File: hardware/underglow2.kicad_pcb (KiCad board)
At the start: 4 copper layers, 78.5 x 95 mm, 96 parts, among them J101 J_Delphi_Sicma_24, J501 Conn_ARM_SWD_TagConnect_TC203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, J502 Conn_ARM_SWD_TagConnect_TC2030, J601 Conn_ARM_SWD_TagConnect_TC203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, Q301 AO4803A, Q302 8205A, Q303 8205A, Q304 8205A, Q305 BCX56, Q306 BCX56, U201 TPS62172DSGR, U301 MCP1416, U302 MCP1416, U303 MCP1416, U304 MCP1416, U305 MCP1416, U306 MCP1416, U307 MCP1416, U308 MCP1416, U401 TLE9251VSJXUMA1, U501 STM32G431CBU6, U601 DA14531-00000FX2, U801 RF69, Y501 32_Mhz, Y601 32_Mhz, Y801 32_Mhz

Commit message: Update layout
Signed-off-by: Connor Rigby <connorr@hey.com>
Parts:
- moved C801 4.50 mm to (31.5, 95.5)
- moved C813 4.50 mm to (27.0, 95.5)
- moved C815 4.50 mm to (39.7, 94.0)
- moved U801 4.50 mm to (35.8, 92.3)
- moved C810 4.50 mm to (29.3, 88.7)
- moved C811 4.50 mm to (29.3, 89.9)
- moved C812 4.50 mm to (29.3, 91.1)
- moved Y801 4.50 mm to (29.3, 94.0)
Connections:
- U501 pad 9: unconnected-(U501-PA1-Pad9) -> /Application/PIXEL_2_PWM
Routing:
- net /Application/PIXEL_2_PWM: track 88.3 -> 130.2 mm, vias 1 -> 4
- net unconnected-(U501-PA1-Pad9): track 22.5 -> 0.00 mm, vias 2 -> 0
- net unconnected-(U501-PA0-Pad8): track 20.4 -> 0.00 mm, vias 2 -> 0
- net unconnected-(U501-PB6-Pad44): track 16.2 -> 0.00 mm, vias 2 -> 0
- net unconnected-(U501-PB7-Pad45): track 15.0 -> 0.00 mm, vias 2 -> 0
- net unconnected-(U501-PC13-Pad2): track 7.10 -> 0.00 mm, vias 1 -> 0
- net /Application/SPI1_SCK: track 24.8 -> 29.6 mm
- net /Application/SPI1_MOSI: track 43.0 -> 47.8 mm
- net /Application/SPI1_RESET: track 39.6 -> 44.1 mm
- net /Application/SPI1_IRQ: track 36.1 -> 40.6 mm
- net /Application/SPI1_MISO: track 25.2 -> 29.7 mm
- net /Application/SPI1_NSS: track 23.2 -> 27.4 mm
- net +3.3V: track 220.8 -> 224.4 mm
- net /Application/RGB1_B_PWM: track 69.4 -> 72.5 mm
- net GND: track 140.1 -> 142.3 mm, vias 56 -> 57
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- removed copper zone on B.Cu, net GND

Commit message: layout updates
Signed-off-by: Connor Rigby <connorr@hey.com>
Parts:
- added ANT601: BWIPX-1-001E, LCSC_Antenna:IPEX-SMD_BWIPX-1-001E, F.Cu at (71.8, 97.0)
- added ANT801: BWSMA-KE-P001, LCSC_Antenna:SMA-SMD_BWSMA-KE-P001, F.Cu at (33.8, 21.6)
- added C605: C_0402_DNP, Capacitor_SMD:C_0402_1005Metric, F.Cu at (77.8, 97.5)
- added C606: C_0402_DNP, Capacitor_SMD:C_0402_1005Metric, F.Cu at (74.6, 97.5)
- added C801: C_0805_10u_X5R, Capacitor_SMD:C_0805_2012Metric, F.Cu at (27.1, 88.7)
- added C802: C_0402_DNP, Capacitor_SMD:C_0402_1005Metric, F.Cu at (35.7, 80.0)
- added C803: C_0402_DNP, Capacitor_SMD:C_0402_1005Metric, F.Cu at (34.7, 80.0)
- added C804: C_0402_DNP, Capacitor_SMD:C_0402_1005Metric, F.Cu at (35.1, 81.5)
- added C805: C_0402_DNP, Capacitor_SMD:C_0402_1005Metric, F.Cu at (33.7, 83.0)
- added C806: C_0402_DNP, Capacitor_SMD:C_0402_1005Metric, F.Cu at (34.7, 85.0)
- added C807: C_0402_DNP, Capacitor_SMD:C_0402_1005Metric, F.Cu at (35.1, 86.5)
- added C808: C_0402_DNP, Capacitor_SMD:C_0402_1005Metric, F.Cu at (33.6, 88.1)
- added C809: C_0402_DNP, Capacitor_SMD:C_0402_1005Metric, F.Cu at (32.5, 88.1)
- added C816: C_0402_DNP, Capacitor_SMD:C_0402_1005Metric, F.Cu at (39.0, 88.1)
- added C817: C_0402_DNP, Capacitor_SMD:C_0402_1005Metric, F.Cu at (37.4, 86.5)
- added C818: C_0402_DNP, Capacitor_SMD:C_0402_1005Metric, F.Cu at (37.9, 85.0)
- added C819: C_0402_DNP, Capacitor_SMD:C_0402_1005Metric, F.Cu at (39.0, 83.0)
- added C820: C_0402_DNP, Capacitor_SMD:C_0402_1005Metric, F.Cu at (37.4, 81.5)
- added C821: C_0402_DNP, Capacitor_SMD:C_0402_1005Metric, F.Cu at (38.9, 80.0)
- added C822: C_0402_DNP, Capacitor_SMD:C_0402_1005Metric, F.Cu at (36.8, 80.0)
- added C823: C_0402_DNP, Capacitor_SMD:C_0402_1005Metric, F.Cu at (36.8, 78.1)
- added C824: C_0402_DNP, Capacitor_SMD:C_0402_1005Metric, F.Cu at (35.7, 78.1)
- added C825: C_0402_DNP, Capacitor_SMD:C_0402_1005Metric, F.Cu at (38.3, 74.3)
- added C826: C_0402_DNP, Capacitor_SMD:C_0402_1005Metric, F.Cu at (34.3, 34.0)
- added C827: C_0402_DNP, Capacitor_SMD:C_0402_1005Metric, F.Cu at (34.3, 31.0)
- added G***: LOGO, LOGO, F.Cu at (56.2, 108.5)
- added L801: L_0402_DNP, Inductor_SMD:L_0402_1005Metric, F.Cu at (33.7, 80.0)
- added L802: L_0402_DNP, Inductor_SMD:L_0402_1005Metric, F.Cu at (34.7, 83.0)
- added L803: L_0402_DNP, Inductor_SMD:L_0402_1005Metric, F.Cu at (34.7, 88.1)
- added L804: L_0402_DNP, Inductor_SMD:L_0402_1005Metric, F.Cu at (35.8, 88.1)
- added L805: L_0402_DNP, Inductor_SMD:L_0402_1005Metric, F.Cu at (36.8, 88.1)
- added L806: L_0402_DNP, Inductor_SMD:L_0402_1005Metric, F.Cu at (37.9, 88.1)
- added L807: L_0402_DNP, Inductor_SMD:L_0402_1005Metric, F.Cu at (37.9, 83.0)
- added L808: L_0402_DNP, Inductor_SMD:L_0402_1005Metric, F.Cu at (37.9, 80.0)
- added Q801: BCX56, Package_TO_SOT_SMD:SOT-89-3, F.Cu at (29.3, 81.8)
- added R601: R_0402_DNP, Resistor_SMD:R_0402_1005Metric, F.Cu at (76.2, 97.0)
- added R801: R_0402_DNP, Resistor_SMD:R_0402_1005Metric, F.Cu at (40.3, 97.2)
- added R802: R_0402_10k, Resistor_SMD:R_0402_1005Metric, F.Cu at (29.9, 85.9)
- added R803: R_0402_DNP, Resistor_SMD:R_0402_1005Metric, F.Cu at (28.8, 85.9)
- added R804: R_0402_DNP, Resistor_SMD:R_0402_1005Metric, F.Cu at (33.8, 32.5)
- added U802: AS193-73LF, Package_TO_SOT_SMD:SOT-363_SC-70-6, F.Cu at (38.8, 76.6)
- renumbered C801 to C814
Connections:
- U801 pad 22: unconnected-(U801-RXTX-Pad22) -> /Radio/RXTX
- U801 pad 24: unconnected-(U801-RFIO-Pad24) -> /Radio/RF_IO
- U801 pad 26: unconnected-(U801-PA_BOOST-Pad26) -> /Radio/PA_BOOST
- U801 pad 27: unconnected-(U801-VR_PA-Pad27) -> /Radio/VR_PA
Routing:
- net /Radio/RXTX: track 0.00 -> 52.1 mm, vias 0 -> 2
- net /Radio/RF69_ANT_MATCH: track 0.00 -> 42.3 mm
- net /Radio/VR_PA: track 0.00 -> 21.6 mm, vias 0 -> 2
- net /Radio/~{RXTX}: track 0.00 -> 17.5 mm
- net GND: track 142.3 -> 156.3 mm, vias 57 -> 129
- net +3.3V: track 224.4 -> 234.3 mm, vias 17 -> 18
- net /Radio/J3: track 0.00 -> 4.98 mm
- net /Radio/RF69_ANTENNA: track 0.00 -> 4.50 mm
- net /BLE/BT_ANT: track 1.21 -> 5.32 mm
- net /Radio/RX_ANT_MATCH: track 0.00 -> 4.06 mm
- net /Radio/TX_ANT_MATCH: track 0.00 -> 3.97 mm
- net /Application/SPI1_RESET: track 44.1 -> 47.9 mm
- net /Radio/RF_IO_MATCH: track 0.00 -> 3.19 mm
- net /Radio/PA_BOOST_MATCH: track 0.00 -> 3.19 mm
- net /Radio/RX_ANT: track 0.00 -> 3.11 mm
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
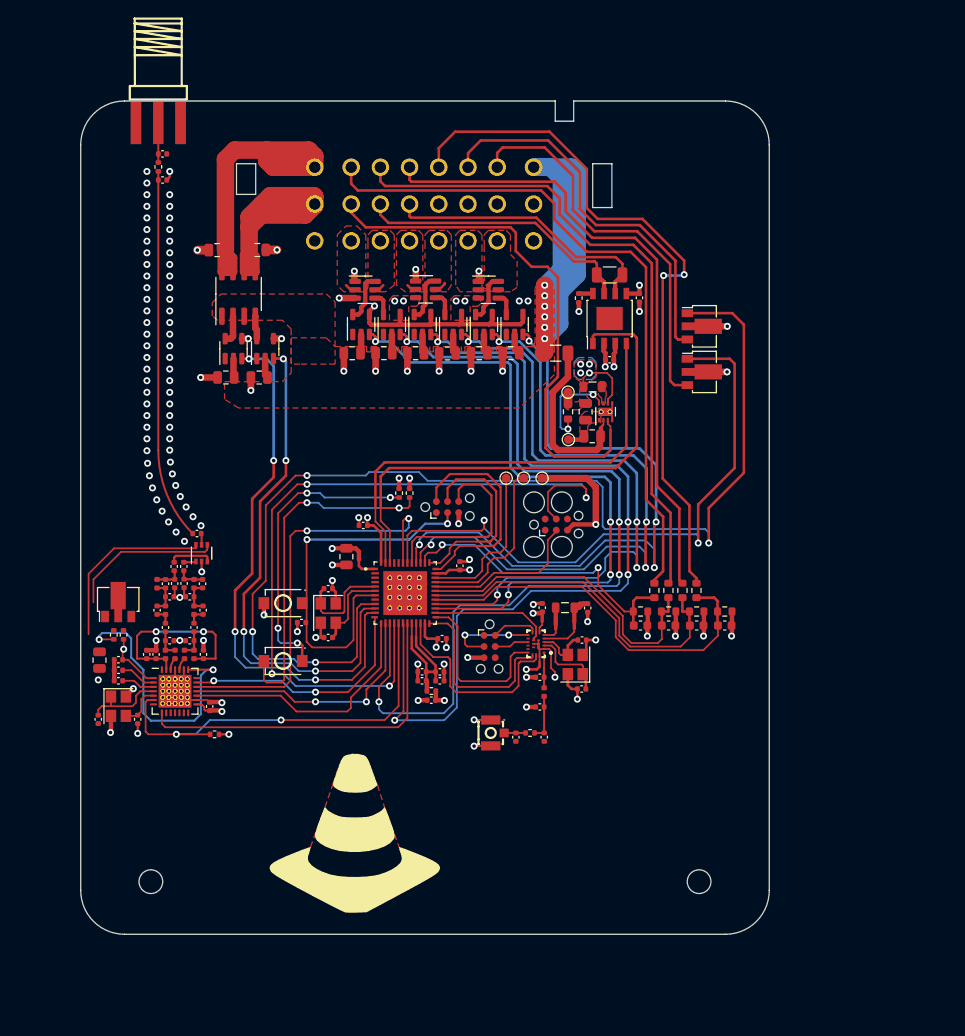
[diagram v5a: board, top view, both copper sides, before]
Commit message: RF layout updates
Signed-off-by: Connor Rigby <connorr@hey.com>
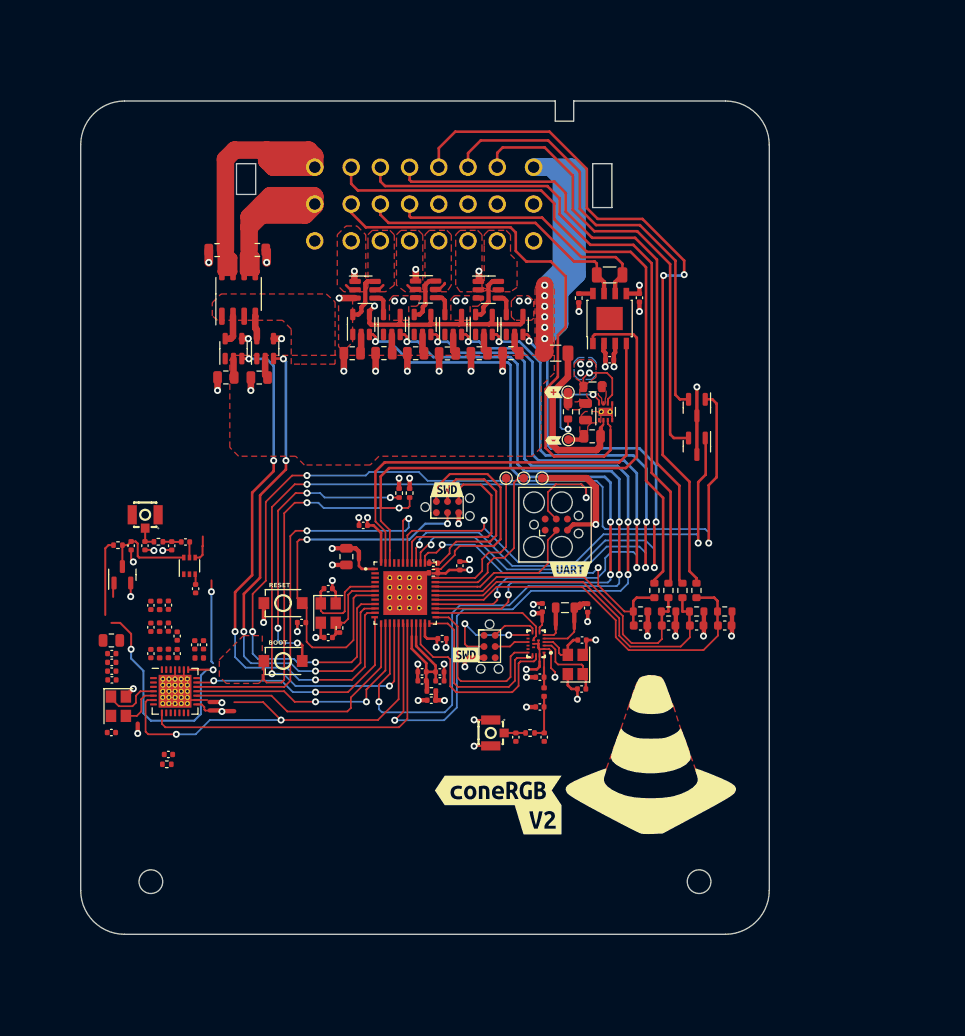
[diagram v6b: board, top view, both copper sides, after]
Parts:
- removed C817, C818, C819, C820, C821, C822, C824: C_0402_DNP, Capacitor_SMD:C_0402_1005Metric
- removed L806, L807, L808: L_0402_DNP, Inductor_SMD:L_0402_1005Metric
- added C828: C_0402_DNP, Capacitor_SMD:C_0402_1005Metric, F.Cu at (30.8, 75.7)
- added C829: C_0402_DNP, Capacitor_SMD:C_0402_1005Metric, F.Cu at (65.2, 77.7)
- added R805: R_0402_10k, Resistor_SMD:R_0402_1005Metric, F.Cu at (65.2, 78.8)
- added kibuzzard-64154474: G***, kibuzzard-64154474, F.Cu at (72.6, 103.6)
- added kibuzzard-6415457F: G***, kibuzzard-6415457F, F.Cu at (77.2, 107.0)
- added kibuzzard-641546EE: G***, kibuzzard-641546EE, F.Cu at (68.9, 88.2)
- added kibuzzard-64154737: G***, kibuzzard-64154737, F.Cu at (80.8, 78.4)
- added kibuzzard-641547A6: G***, kibuzzard-641547A6, F.Cu at (66.8, 69.3)
- added kibuzzard-64155347: G***, kibuzzard-64155347, F.Cu at (78.9, 58.2)
- added kibuzzard-641553AB: G***, kibuzzard-641553AB, F.Cu at (78.9, 63.7)
- ANT801: value BWSMA-KE-P001 -> BWIPX-1-001E; footprint LCSC_Antenna:SMA-SMD_BWSMA-KE-P001 -> LCSC_Antenna:IPEX-SMD_BWIPX-1-001E
- C801: value C_0805_10u_X5R -> C_0402_DNP; footprint Capacitor_SMD:C_0805_2012Metric -> Capacitor_SMD:C_0402_1005Metric
- C808, C809, C813: value C_0402_DNP -> C_0402_100nf_X7R
- C811, C812, C815: value C_0402_100nf_X7R -> C_0402_DNP
- C816: value C_0402_DNP -> C_0805_10u_X5R; footprint Capacitor_SMD:C_0402_1005Metric -> Capacitor_SMD:C_0805_2012Metric
- L801: value L_0402_DNP -> 2.7nh
- L802: value L_0402_DNP -> 22nh
- L803, L804, L805: value L_0402_DNP -> 5.6nh
- Q305, Q306, Q801: value BCX56 -> BC817; footprint Package_TO_SOT_SMD:SOT-89-3 -> Package_TO_SOT_SMD:SOT-23
- moved ANT801 50.7 mm to (32.4, 72.2)
- moved C827 44.7 mm to (32.3, 75.7), turned to 90 degrees
- moved R804 42.7 mm to (33.9, 75.2), turned to 180 degrees
- moved C826 41.7 mm to (35.4, 75.7), turned to 90 degrees
- moved G*** 34.9 mm to (90.0, 99.5)
- moved R803 25.7 mm to (54.5, 85.1)
- moved C814 11.3 mm to (39.0, 87.0)
- moved C816 10.6 mm to (28.5, 86.5), turned to 180 degrees
- moved R802 10.2 mm to (29.2, 75.6), turned to 0 degrees
- moved Q306 9.28 mm to (95.2, 60.0), turned to -90 degrees
- moved C813 8.94 mm to (35.0, 99.5), turned to 0 degrees
- moved Q305 8.49 mm to (95.2, 64.4), turned to -90 degrees
- moved L801 8.05 mm to (35.0, 88.0), turned to 90 degrees
- moved C802 7.99 mm to (36.0, 88.0)
- moved C815 7.22 mm to (38.0, 87.0), turned to -90 degrees
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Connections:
- ANT801 pad 1: GND -> /Radio/RF69_ANTENNA
- C801 pad 1: +3.3V -> /Radio/VR_PA
- C802 pad 1: /Radio/TX_ANT -> Net-(C802-Pad1)
- C803 pad 1: /Radio/TX_ANT -> Net-(C802-Pad1)
- C803 pad 2: /Radio/TX_ANT_MATCH -> Net-(C803-Pad2)
- C804 pad 1: /Radio/TX_ANT_MATCH -> Net-(C803-Pad2)
- C804 pad 2: GND -> Net-(C804-Pad2)
- C805 pad 1: /Radio/TX_ANT_MATCH -> GND
- C805 pad 2: /Radio/PA_BOOST_RF -> Net-(C804-Pad2)
- C806 pad 1: /Radio/PA_BOOST_RF -> Net-(C804-Pad2)
- C806 pad 2: /Radio/PA_BOOST_MATCH -> /Radio/J2
- C807 pad 1: /Radio/PA_BOOST_MATCH -> GND
- C807 pad 2: GND -> /Radio/J2
- C808 pad 1: /Radio/VR_PA -> +3.3V
- C809 pad 1: /Radio/VR_PA -> /Radio/VR_ANA
- C810 pad 1: +3.3V -> /Radio/VR_DIG
- C811 pad 1: /Radio/VR_ANA -> /Radio/XTA
- C812 pad 1: /Radio/VR_DIG -> /Radio/XTB
- C813 pad 1: /Radio/XTA -> +3.3V
- C814 pad 1: /Radio/XTB -> Net-(C814-Pad1)
- C815 pad 1: +3.3V -> Net-(C814-Pad1)
- C815 pad 2: GND -> /Radio/RF_IO
- C816 pad 1: /Radio/VR_PA -> +3.3V
- C823 pad 1: /Radio/RX_ANT -> Net-(C814-Pad1)
- C823 pad 2: /Radio/J2 -> /Radio/J3
- C825 pad 1: /Radio/J1 -> unconnected-(C825-Pad1)
- L801 pad 1: /Radio/TX_ANT -> /Radio/PA_BOOST
- L801 pad 2: /Radio/TX_ANT_MATCH -> Net-(C802-Pad1)
- L802 pad 1: /Radio/TX_ANT_MATCH -> /Radio/VR_PA
- L802 pad 2: /Radio/PA_BOOST_RF -> Net-(C802-Pad1)
- L803 pad 1: /Radio/PA_BOOST_MATCH -> Net-(C803-Pad2)
- L803 pad 2: /Radio/VR_PA -> Net-(C804-Pad2)
- L804 pad 1: /Radio/PA_BOOST_MATCH -> Net-(C804-Pad2)
- L804 pad 2: /Radio/PA_BOOST -> /Radio/J2
- L805 pad 1: /Radio/RF_IO -> GND
- L805 pad 2: /Radio/RF_IO_MATCH -> /Radio/RF_IO
- Q305 pad 2: +3.3V -> /RGB/PIXEL_1
- Q305 pad 3: /RGB/PIXEL_1 -> +3.3V
- Q306 pad 2: +3.3V -> /RGB/PIXEL_2
- Q306 pad 3: /RGB/PIXEL_2 -> +3.3V
- Q801 pad 1: /Radio/RXTX_INV -> unconnected-(Q801-B-Pad1)
- Q801 pad 2: /Radio/~{RXTX} -> GND
- Q801 pad 3: GND -> Net-(Q801-C)
- R802 pad 2: /Radio/~{RXTX} -> Net-(Q801-C)
- U802 pad 4: /Radio/~{RXTX} -> unconnected-(U802-V2-Pad4)
- U802 pad 5: /Radio/J1 -> unconnected-(U802-J1-Pad5)
- U802 pad 6: /Radio/RXTX -> Net-(Q801-C)
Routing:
- net /Radio/RF69_ANT_MATCH: track 42.3 -> 2.12 mm
- net /Radio/RXTX: track 52.1 -> 28.5 mm
- net /Radio/VR_PA: track 21.6 -> 0.00 mm, vias 2 -> 0
- net /Radio/~{RXTX}: track 17.5 -> 0.00 mm
- net /Application/PIXEL_2_PWM: track 130.2 -> 114.6 mm
- net /Application/PIXEL_1_PWM: track 70.1 -> 54.6 mm
- net Net-(Q801-C): track 0.00 -> 11.2 mm
- net unconnected-(R805-Pad1): track 0.00 -> 9.54 mm, vias 0 -> 1
- net GND: track 156.3 -> 148.4 mm, vias 129 -> 62
- net /RGB/PIXEL_2: track 44.2 -> 51.0 mm
- net /RGB/PIXEL_1: track 44.9 -> 51.1 mm
- net /Radio/VR_ANA: track 4.09 -> 0.00 mm
- net /Radio/RX_ANT_MATCH: track 4.06 -> 0.00 mm
- net /Radio/TX_ANT_MATCH: track 3.97 -> 0.00 mm
- net /Radio/VR_DIG: track 3.80 -> 0.00 mm
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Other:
- board text added: "BOOT"
- board text added: "RESET"

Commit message: Almost ready for fab
Signed-off-by: Connor Rigby <connorr@hey.com>
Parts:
- added D201: LED_0603_RED, LED_SMD:LED_0603_1608Metric, F.Cu at (78.9, 62.4)
- added D501: LED_0603_GREEN, LED_SMD:LED_0603_1608Metric, F.Cu at (50.7, 78.6)
- added D502: LED_0603_YELLOW, LED_SMD:LED_0603_1608Metric, F.Cu at (52.3, 78.6)
- added R201: R_0603_330, Resistor_SMD:R_0603_1608Metric, F.Cu at (78.9, 59.3)
- added R503: R_0603_330, Resistor_SMD:R_0603_1608Metric, F.Cu at (50.7, 75.5)
- added R504: R_0603_330, Resistor_SMD:R_0603_1608Metric, F.Cu at (52.3, 75.5)
- added kibuzzard-6418DACD: G***, kibuzzard-6418DACD, F.Cu at (48.6, 74.8)
- added kibuzzard-6418DAF6: G***, kibuzzard-6418DAF6, F.Cu at (54.5, 74.8)
- added kibuzzard-6418DF1A: G***, kibuzzard-6418DF1A, F.Cu at (76.5, 63.0)
- C503, C504, C603, C604, C811, C812: value C_0402_DNP -> C_0402_33p_C0G
- C801: value C_0402_DNP -> C_0402_10n_C0G
- C802: value C_0402_DNP -> C_0402_8p2_C0G
- C803: value C_0402_DNP -> C_0402_22p_C0G
- C805: value C_0402_DNP -> C_0402_6p8_C0G
- C807: value C_0402_DNP -> C_0402_3p3_C0G
- C814: value C_0402_DNP -> C_0402_5p6_C0G
- C815: value C_0402_DNP -> L_0402_5n6; footprint Capacitor_SMD:C_0402_1005Metric -> Inductor_SMD:L_0402_1005Metric
- C823, C825: value C_0402_DNP -> C_0402_100p_C0G
- C828, C829: value C_0402_DNP -> C_0402_1nf_X7R
- L501, R601, R804: value R_0402_DNP -> R_0402_0
- L801: value 2.7nh -> L_0402_2n7
- L802: value 22nh -> L_0402_22n
- L803, L804: value 5.6nh -> L_0402_5n6
- L805: value 5.6nh -> L_0402_120n
- R701, R703, R705, R707: value DNP -> R_0603_100k
- R702, R704, R706, R708: value DNP -> R_0603_20k
- R801, R803: value R_0402_DNP -> R_0402_100k
- R802: value R_0402_10k -> R_0402_100k
- moved R805 35.0 mm to (31.0, 86.0), turned to 90 degrees
- moved C829 26.5 mm to (38.7, 78.8)
- moved R803 16.7 mm to (38.7, 79.8), turned to 180 degrees
- moved R801 10.0 mm to (42.2, 93.8), turned to 90 degrees
- moved C813 7.48 mm to (39.9, 93.8), turned to 90 degrees
- moved C828 5.03 mm to (29.2, 80.5), turned to 0 degrees
- moved C823 4.00 mm to (38.1, 84.6)
- moved Q801 4.00 mm to (29.8, 83.0)
- moved U802 4.00 mm to (37.4, 82.0)
- moved R802 3.85 mm to (29.2, 79.5)
- moved kibuzzard-64155347 2.37 mm to (80.5, 56.5), turned to -90 degrees
- moved C825 2.35 mm to (36.9, 77.6)
- moved C826 2.35 mm to (35.4, 78.1)
- moved ANT801 2.35 mm to (32.4, 74.6)
- moved C827 2.35 mm to (32.3, 78.0)
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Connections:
- net Net-(ANT601-SIG) renamed /BLE/BLE_ANT
- net Net-(C802-Pad1) renamed /Radio/PA_BOOST_PA
- net Net-(C803-Pad2) renamed /Radio/PA_BOOST_PA_MATCH
- net Net-(C804-Pad2) renamed /Radio/PA_BOOST_PA_FILTER
- net Net-(C814-Pad1) renamed /Radio/RFIO_MATCH
- net Net-(Q801-C) renamed /Radio/V1
- C825 pad 1: unconnected-(C825-Pad1) -> /Radio/J1
- C829 pad 1: unconnected-(C829-Pad1) -> GND
- C829 pad 2: unconnected-(C829-Pad2) -> /Radio/V2
- Q801 pad 1: unconnected-(Q801-B-Pad1) -> /Radio/RXTX_NOR
- R803 pad 2: /Radio/RXTX_INV -> /Radio/V2
- R805 pad 1: unconnected-(R805-Pad1) -> /Radio/RXTX
- R805 pad 2: /Radio/~{RXTX} -> /Radio/RXTX_NOR
- U501 pad 44: unconnected-(U501-PB6-Pad44) -> /Application/LED_GREEN
- U501 pad 45: unconnected-(U501-PB7-Pad45) -> /Application/LED_YELLOW
- U802 pad 4: unconnected-(U802-V2-Pad4) -> /Radio/V2
- U802 pad 5: unconnected-(U802-J1-Pad5) -> /Radio/J1
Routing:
- net +3.3V: track 233.7 -> 269.4 mm, vias 15 -> 17
- net GND: track 148.4 -> 179.1 mm, vias 62 -> 96
- net /Application/LED_GREEN: track 0.00 -> 16.6 mm, vias 0 -> 2
- net /Application/LED_YELLOW: track 0.00 -> 12.5 mm, vias 0 -> 2
- net unconnected-(R805-Pad1): track 9.54 -> 0.00 mm, vias 1 -> 0
- net /Radio/RXTX: track 28.5 -> 35.5 mm, vias 2 -> 3
- net /Radio/VR_ANA: track 0.00 -> 5.22 mm
- net /Radio/VR_DIG: track 0.00 -> 5.02 mm
- net /Radio/PA_BOOST_PA_FILTER: track 0.00 -> 4.51 mm
- net /Radio/J2: track 0.00 -> 4.47 mm
- net /Radio/RF_IO: track 0.00 -> 3.67 mm
- net /Power/EN: track 61.8 -> 65.4 mm
- net /Radio/VR_PA: track 0.00 -> 3.51 mm
- net /Radio/J1: track 0.00 -> 3.40 mm
- net /Radio/RXTX_NOR: track 0.00 -> 3.28 mm
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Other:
- board text added: "Rev. 1"

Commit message: Pre-production updates
Signed-off-by: Connor Rigby <connorr@hey.com>
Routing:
- net /Application/USART1_TX: track 88.0 -> 88.7 mm
